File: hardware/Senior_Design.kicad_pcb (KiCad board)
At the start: 4 copper layers, 134.1 x 88 mm, 152 parts, among them J101 Conn_ARM_JTAG_SWD_10, J201 54-00125, J202 Conn_01x03, J301 Conn_ARM_JTAG_SWD_10, J501 2305018-2, J601 J0011D21BNL, Q201 CSD87503Q3E, Q202 Q_NMOS, Q203 CSD87503Q3E, SW101 SW_Push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

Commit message: PCB layout update
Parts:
- C406, C407, D301, R302, U402, U403, U502: moved to B.Cu
- C501, C502: footprint Capacitor_SMD:C_0805_2012Metric -> Capacitor_SMD:C_0603_1608Metric
- R505: moved to F.Cu
- moved SW201 49.4 mm to (7.90, -13.5), turned to 0 degrees
- moved R210 46.4 mm to (10.6, -17.1), turned to 180 degrees
- moved R505 38.6 mm to (65.9, -38.5), turned to 90 degrees
- moved R203 35.8 mm to (27.4, -31.0), turned to 90 degrees
- moved C209 35.5 mm to (27.3, -23.0)
- moved R508 35.4 mm to (59.1, -35.5)
- moved D503 35.3 mm to (59.1, -37.5)
- moved R504 35.0 mm to (68.0, -38.5), turned to -90 degrees
- moved D204 34.7 mm to (12.4, -22.9)
- moved R205 34.7 mm to (14.9, -22.8)
- moved J501 34.0 mm to (78.9, -41.8)
- moved D203 33.6 mm to (23.0, -21.2)
- moved R506 33.5 mm to (76.2, -35.5), turned to 0 degrees
- moved C501 33.1 mm to (60.3, -43.9), turned to -135 degrees
- moved D501 32.8 mm to (71.8, -36.5), turned to -90 degrees
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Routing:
- net USB_VBUS: track 24.2 -> 96.9 mm, vias 0 -> 12
- net /MCU/MCU_RX_CP_TX: track 0.00 -> 46.2 mm
- net /MCU/MCU_TX_CP_RX: track 0.00 -> 46.1 mm
- net /BMS/VAC2: track 62.7 -> 29.7 mm, vias 1 -> 2
- net /BMS/BQ_INT: track 1.16 -> 19.7 mm, vias 1 -> 2
- net Net-(C204-Pad1): track 29.4 -> 47.6 mm, vias 0 -> 1
- net /MCU/BDE_RST: track 38.6 -> 21.8 mm
- net Net-(U201-PROG): track 1.74 -> 18.6 mm, vias 1 -> 2
- net Net-(SPS30_Connector401-Pin_2): track 0.00 -> 15.3 mm
- net Net-(SPS30_Connector401-Pin_3): track 0.00 -> 13.4 mm
- net /MCU/nRST: track 37.8 -> 24.8 mm, vias 4 -> 3
- net /Wi-SUN Module/JTAG_TCKC: track 21.8 -> 10.5 mm, vias 3 -> 0
- net /BMS/QON: track 0.79 -> 11.8 mm, vias 0 -> 1
- net Net-(D203-K): track 0.00 -> 10.2 mm
- net Net-(J501-SHIELD-PadSH1): track 15.3 -> 5.10 mm
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- removed copper zone on In2.Cu, net +3.3V
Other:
- board size 134.1 x 88 mm -> 120.5 x 71.5 mm

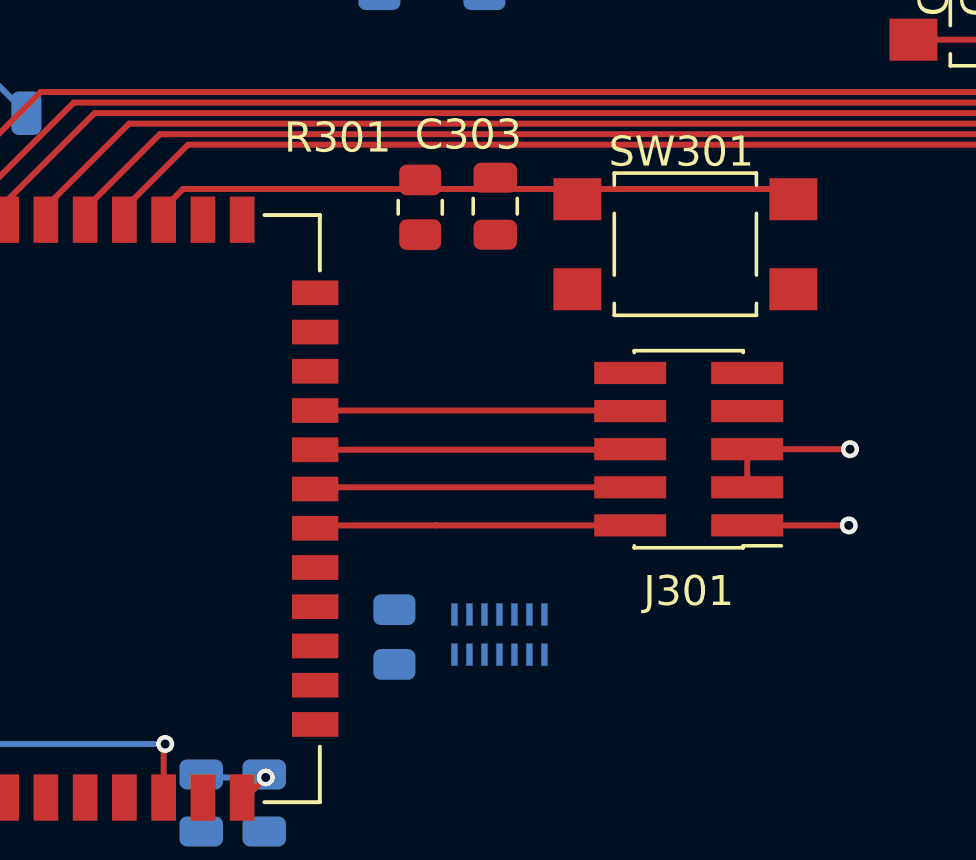
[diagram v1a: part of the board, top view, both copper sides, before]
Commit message: BDE JTAG layout
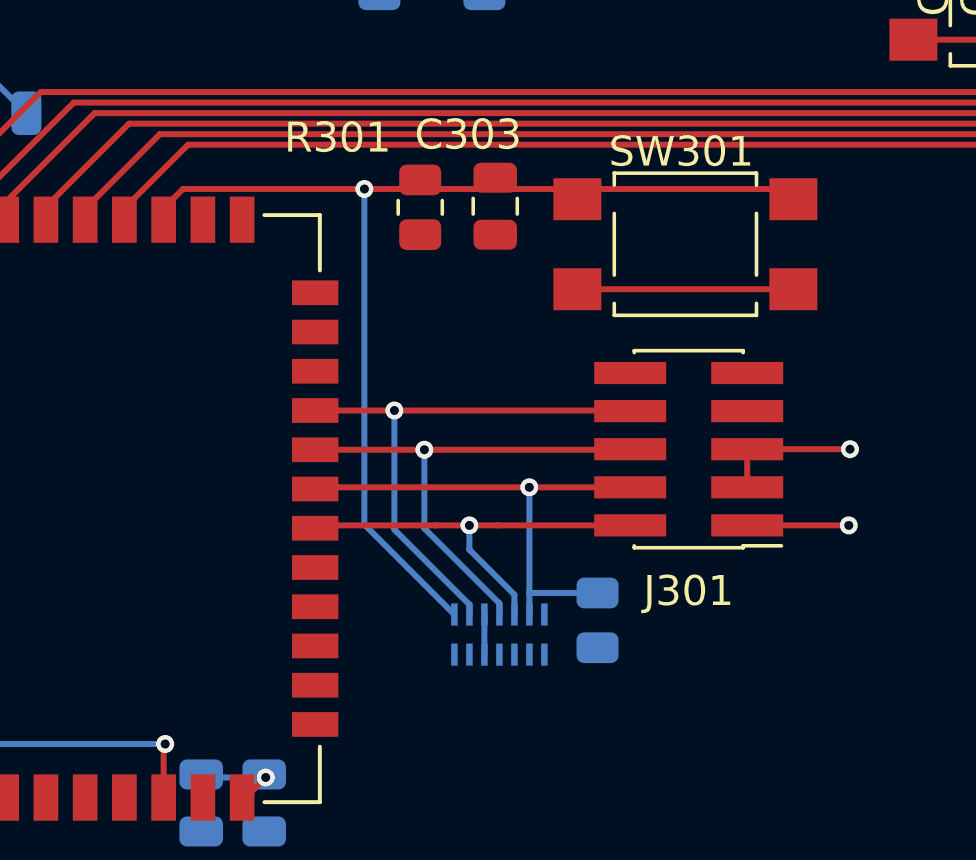
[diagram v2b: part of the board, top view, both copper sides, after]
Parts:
- moved R302 6.79 mm to (-6.23, 7.35)
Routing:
- net /MCU/BDE_RST: track 21.8 -> 37.2 mm, vias 0 -> 1
- net GND: track 138.7 -> 147.2 mm
- net /Wi-SUN Module/JTAG_TDI: track 10.5 -> 18.3 mm, vias 0 -> 1
- net /Wi-SUN Module/JTAG_TDO: track 10.5 -> 17.0 mm, vias 0 -> 1
- net /Wi-SUN Module/JTAG_TCKC: track 10.5 -> 17.0 mm, vias 0 -> 1
- net /Wi-SUN Module/JTAG_TMSC: track 10.5 -> 14.1 mm, vias 0 -> 1
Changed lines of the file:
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@@
 	(footprint "Resistor_SMD:R_0805_2012Metric"
 		(layer "B.Cu")
-		(at -13 7.9125 90)
+		(at -6.228401 7.35481 90)
 		(descr "Resistor SMD 0805 (2012 Metric), square (rectangular) end terminal, IPC-7351 nominal, (Body size source: IPC-SM-782 page 72, https://www.pcb-3d.com/wordpress/wp-content/uploads/ipc-sm-782a_amendment_1_and_2.pdf), generated with kicad-footprint-generator")
 		(tags "resistor")
@@
 	)
 	(segment
+		(start -6.901025 -3.682283)
+		(end 0.298975 -3.682283)
+		(width 0.2)
+		(layer "F.Cu")
+		(net 1)
+	)
+	(segment
 		(start 7.7 -30.9)
 		(end 7.110741 -30.9)
@@
 	)
 	(segment
+		(start -10 7.16)
+		(end -10 8.5)
+		(width 0.2)
+		(layer "B.Cu")
+		(net 1)
+	)
+	(segment
 		(start -33.63975 -3.52355)
 		(end -31.63975 -3.52355)
@@
 	(segment
 		(start -20.0468 -7.0235)
+		(end -14 -7.0235)
+		(width 0.2)
+		(layer "F.Cu")
+		(net 13)
+	)
+	(segment
+		(start -14 -7.0235)
 		(end -0.042242 -7.0235)
 		(width 0.2)
@@
 		(net 13)
 	)
+	(via
+		(at -14 -7.0235)
+		(size 0.6)
+		(drill 0.3)
+		(layers "F.Cu" "B.Cu")
+		(net 13)
+	)
+	(segment
+		(start -11 7.16)
+		(end -14 4.16)
+		(width 0.2)
+		(layer "B.Cu")
+		(net 13)
+	)
+	(segment
+		(start -14 4.16)
+		(end -14 -7.0235)
+		(width 0.2)
+		(layer "B.Cu")
+		(net 13)
+	)
 	(segment
 		(start -25.268738 -9.549821)
@@
 	)
 	(segment
-		(start -5.13975 4.19)
-		(end -11.63975 4.19)
+		(start -9.548371 4.19)
+		(end -10.5 4.19)
 		(width 0.2)
 		(layer "F.Cu")
@@
 	)
 	(segment
+		(start -10.5 4.19)
+		(end -11.63975 4.19)
+		(width 0.2)
+		(layer "F.Cu")
+		(net 78)
+	)
+	(segment
+		(start -5.13975 4.19)
+		(end -9.548371 4.19)
+		(width 0.2)
+		(layer "F.Cu")
+		(net 78)
+	)
+	(segment
 		(start -15.5452 4.19)
 		(end -15.63975 4.28455)
@@
 		(net 78)
 	)
+	(via
+		(at -10.5 4.19)
+		(size 0.6)
+		(drill 0.3)
+		(layers "F.Cu" "B.Cu")
+		(net 78)
+	)
 	(segment
-		(start -15.63975 1.66835)
+		(start -9 6.5)
+		(end -10.5 5)
+		(width 0.2)
+		(layer "B.Cu")
+		(net 78)
+	)
+	(segment
+		(start -9 7.16)
+		(end -9 6.5)
+		(width 0.2)
+		(layer "B.Cu")
+		(net 78)
+	)
+	(segment
+		(start -10.5 5)
+		(end -10.5 4.19)
+		(width 0.2)
+		(layer "B.Cu")
+		(net 78)
+	)
+	(segment
+		(start -12 1.66835)
 		(end -5.1581 1.66835)
 		(width 0.2)
@@
 	)
 	(segment
-		(start -15.63975 0.36025)
+		(start -15.63975 1.66835)
+		(end -12 1.66835)
+		(width 0.2)
+		(layer "F.Cu")
+		(net 79)
+	)
+	(via
+		(at -12 1.66835)
+		(size 0.6)
+		(drill 0.3)
+		(layers "F.Cu" "B.Cu")
+		(net 79)
+	)
+	(segment
+		(start -9.5 6.790001)
+		(end -9.5 7.16)
+		(width 0.2)
+		(layer "B.Cu")
+		(net 79)
+	)
+	(segment
+		(start -12 4.290001)
+		(end -9.5 6.790001)
+		(width 0.2)
+		(layer "B.Cu")
+		(net 79)
+	)
+	(segment
+		(start -12 1.66835)
+		(end -12 4.290001)
+		(width 0.2)
+		(layer "B.Cu")
+		(net 79)
+	)
+	(segment
+		(start -13 0.36025)
 		(end -5.1595 0.36025)
 		(width 0.2)
@@
 	)
 	(segment
+		(start -15.63975 0.36025)
+		(end -13 0.36025)
+		(width 0.2)
+		(layer "F.Cu")
+		(net 80)
+	)
+	(via
+		(at -13 0.36025)
+		(size 0.6)
+		(drill 0.3)
+		(layers "F.Cu" "B.Cu")
+		(net 80)
+	)
+	(segment
+		(start -13 4.328716)
+		(end -10.5 6.828716)
+		(width 0.2)
+		(layer "B.Cu")
+		(net 80)
+	)
+	(segment
+		(start -10.5 6.828716)
+		(end -10.5 7.16)
+		(width 0.2)
+		(layer "B.Cu")
+		(net 80)
+	)
+	(segment
+		(start -13 0.36025)
+		(end -13 4.328716)
+		(width 0.2)
+		(layer "B.Cu")
+		(net 80)
+	)
+	(segment
 		(start -15.5833 2.92)
 		(end -15.63975 2.97645)
@@
 	)
 	(segment
-		(start -5.13975 2.92)
+		(start -8.503519 2.92)
 		(end -15.5833 2.92)
 		(width 0.2)
@@
 		(net 81)
 	)
+	(segment
+		(start -5.13975 2.92)
+		(end -8.503519 2.92)
+		(width 0.2)
+		(layer "F.Cu")
+		(net 81)
+	)
+	(via
+		(at -8.503519 2.92)
+		(size 0.6)
+		(drill 0.3)
+		(layers "F.Cu" "B.Cu")
+		(net 81)
+	)
+	(segment
+		(start -8.5 7.16)
+		(end -8.5 6.441148)
+		(width 0.2)
+		(layer "B.Cu")
+		(net 81)
+	)
+	(segment
+		(start -8.498838 6.44231)
+		(end -8.5 6.441148)
+		(width 0.2)
+		(layer "B.Cu")
+		(net 81)
+	)
+	(segment
+		(start -6.228401 6.44231)
+		(end -8.498838 6.44231)
+		(width 0.2)
+		(layer "B.Cu")
+		(net 81)
+	)
+	(segment
+		(start -8.5 2.923519)
+		(end -8.503519 2.92)
+		(width 0.2)
+		(layer "B.Cu")
+		(net 81)
+	)
+	(segment
+		(start -8.5 6.441148)
+		(end -8.5 2.923519)
+		(width 0.2)
+		(layer "B.Cu")
+		(net 81)
+	)

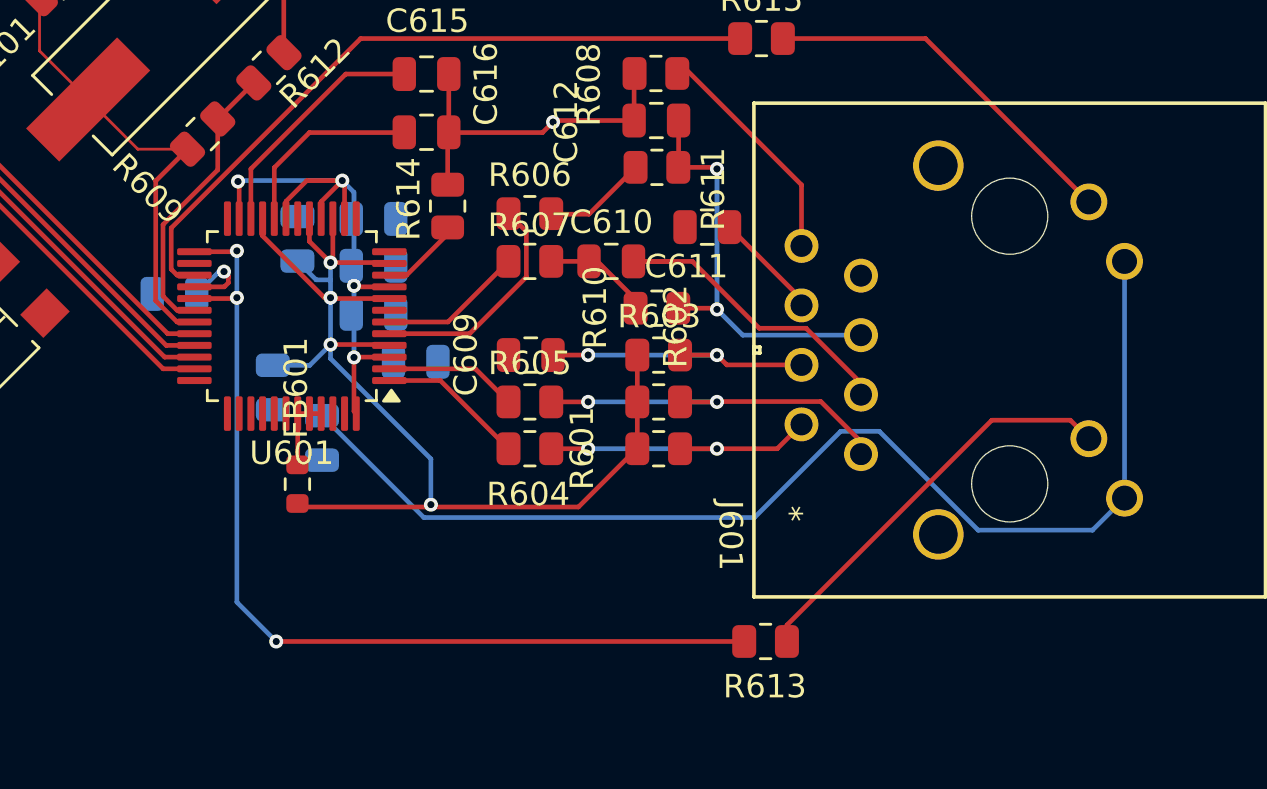
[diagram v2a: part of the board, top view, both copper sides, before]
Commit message: ethernet cap layout
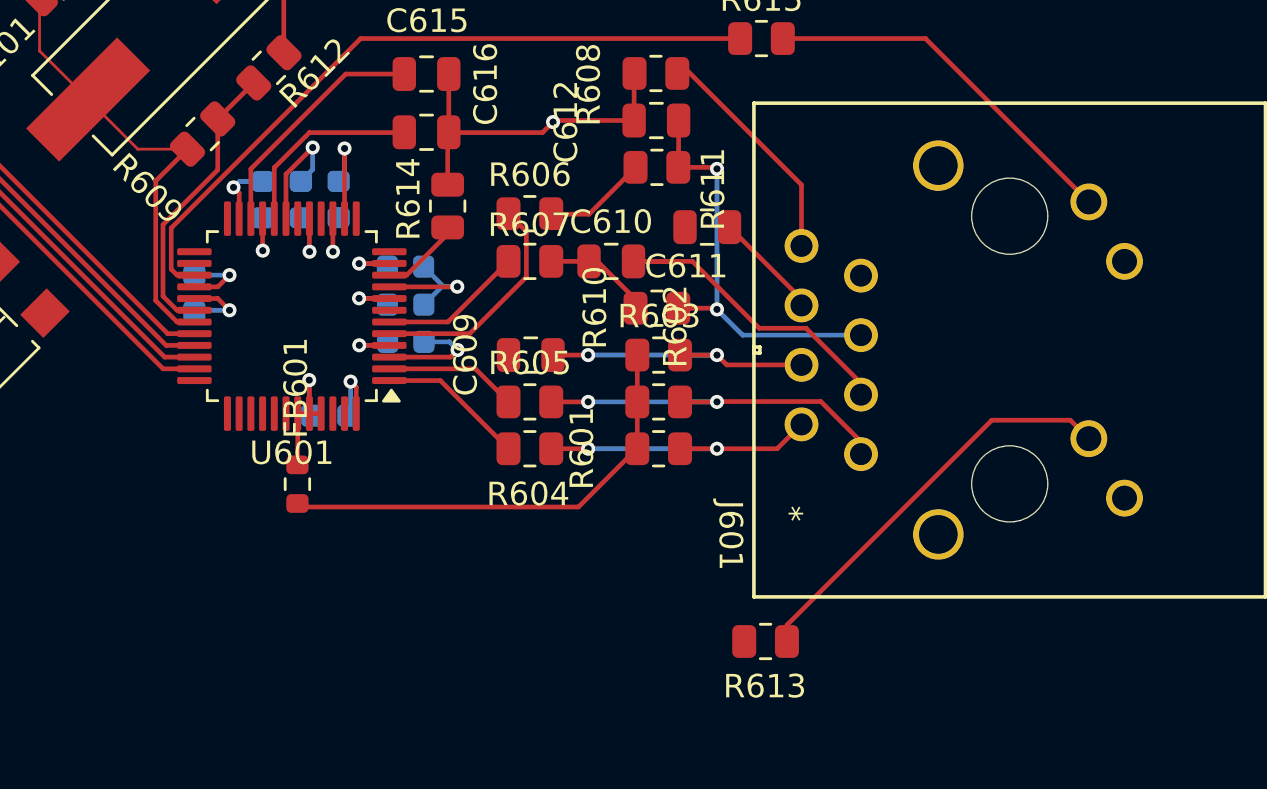
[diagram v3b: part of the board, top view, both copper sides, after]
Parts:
- C601, C602, C603, C604, C605, C606, C607, C608: footprint Capacitor_SMD:C_0805_2012Metric -> Capacitor_SMD:C_0603_1608Metric
- moved C608 9.51 mm to (39.9, -8.22), turned to 90 degrees
- moved C604 8.12 mm to (41.5, -8.23), turned to 90 degrees
- moved C603 5.43 mm to (46.0, -2.15)
- moved C605 5.41 mm to (46.0, -3.74), turned to 0 degrees
- moved C607 5.10 mm to (43.2, -8.23), turned to 90 degrees
- moved C606 1.37 mm to (46.0, -5.36)
- moved C602 1.00 mm to (42.8, 1.00), turned to 0 degrees
- moved C601 0.85 mm to (37.0, -4.22), turned to -90 degrees
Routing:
- net +3.3V: track 69.0 -> 21.6 mm, vias 5 -> 6
- net /Ethernet/LINKLED: track 39.2 -> 0.00 mm, vias 2 -> 0
- net +3.3VA: track 65.3 -> 32.0 mm, vias 4 -> 6
- net GND: track 147.2 -> 160.9 mm, vias 42 -> 44

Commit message: PCB_layout_957pm_Mar11
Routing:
- net GND: track 160.9 -> 162.3 mm, vias 44 -> 45
- net Net-(U202-L2_6): track 0.00 -> 0.50 mm
- net Net-(U202-L1_8): track 0.00 -> 0.50 mm
- added copper zone on F.Cu, net +3.3V
- added copper zone on F.Cu, net /BMS/PMID
- added copper zone on F.Cu, net /BMS/SYS
- added copper zone on B.Cu, net GND
- added copper zone on In1.Cu, net GND
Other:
- board size 120.5 x 71.5 mm -> 117.8 x 71.5 mm

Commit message: PCB update
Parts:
- C101, C102, C103, C104, C106, C107: footprint Capacitor_SMD:C_0805_2012Metric -> Capacitor_SMD:C_0603_1608Metric
- C108, C109: footprint Capacitor_SMD:C_0805_2012Metric -> Capacitor_SMD:C_0603_1608Metric; moved to B.Cu
- D104, R203, R209: moved to B.Cu
- R101, R102: moved to F.Cu
- moved R203 133.8 mm to (87.6, -150.5), turned to 180 degrees
- moved R209 132.1 mm to (87.6, -152.5), turned to 180 degrees
- moved R102 108.4 mm to (32.5, -114.1), turned to -90 degrees
- moved U403 107.9 mm to (20.5, -116.5)
- moved C406 107.6 mm to (23.3, -105.0)
- moved C407 107.6 mm to (19.8, -105.0)
- moved U402 107.6 mm to (21.6, -108.2)
- moved R612 106.5 mm to (92.0, -106.9)
- moved R609 106.5 mm to (89.2, -104.1)
- moved C201 106.5 mm to (60.4, -130.7)
- moved C202 106.5 mm to (60.4, -129.1)
- moved C203 106.5 mm to (35.7, -129.4)
- moved C204 106.5 mm to (60.4, -115.3)
- moved C205 106.5 mm to (60.4, -117.5)
- moved C206 106.5 mm to (60.0, -120.5)
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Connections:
- C405 pad 1: Net-(D401-A) -> GND
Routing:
- net /BME 688 and SPS30/SDA: track 8.13 -> 79.7 mm, vias 0 -> 3
- net /BME 688 and SPS30/SCL: track 8.28 -> 78.9 mm, vias 0 -> 3
- net USB_VBUS: track 96.9 -> 55.4 mm
- net Net-(C204-Pad1): track 47.6 -> 8.92 mm
- net /Ethernet/ACTLED: track 30.5 -> 0.00 mm
- net /MCU/nRST: track 24.8 -> 53.7 mm, vias 3 -> 2
- net /MCU/JTAG_TDI: track 10.6 -> 35.3 mm, vias 2 -> 1
- net /MCU/JTAG_TDO: track 10.8 -> 34.4 mm, vias 2 -> 1
- net /BMS/QON: track 11.8 -> 35.1 mm, vias 1 -> 2
- net /MCU/JTAG_TCK: track 10.9 -> 33.7 mm, vias 2 -> 1
- net /MCU/BDE_RST: track 37.2 -> 59.9 mm
- net Net-(Q202-G): track 20.7 -> 1.48 mm
- net /MCU/JTAG_TMS: track 13.5 -> 32.7 mm, vias 2 -> 1
- net GND: track 162.3 -> 143.4 mm, vias 45 -> 42
- net Net-(U201-PROG): track 18.6 -> 1.79 mm, vias 2 -> 1
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- added copper zone on F.Cu, net (none)
- added copper zone on F.Cu, net +5V
- added copper zone on F.Cu, net BAT
- added copper zone on F.Cu, net GND
- added copper zone on F.Cu, net Net-(C204-Pad1)
- added copper zone on F.Cu, net Net-(C401-Pad2)
- added copper zone on F.Cu, net Net-(D401-A)
- added copper zone on B.Cu, net Net-(U201-SW1)
- added copper zone on F.Cu, net Net-(U201-SW1)
- added copper zone on F.Cu, net Net-(U201-SW2)
- added copper zone on F.Cu, net Net-(U202-L1_8)
- added copper zone on F.Cu, net Net-(U202-L2_6)
- removed copper zone on B.Cu, net GND
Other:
- board size 117.8 x 71.5 mm -> 121.3 x 71.5 mm
